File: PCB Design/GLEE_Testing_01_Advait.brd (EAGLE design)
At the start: 41.8 x 42.9 mm, 53 parts, among them IC1 SI7021, IC2 ATMEGA328-PB, IC3 PE4259, U1 V_REG_317SMD, U2 LSM9DS1, X1 LTI-SASF54GT, Y1 16MHz, Y2 32Mhz

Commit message: Final QA
Added a few changes, updated filenames, added library and BOM
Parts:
- removed C31: nc, SparkFun:0402-CAP
- added C26: 100nF, SparkFun:0402-CAP
- added R6: 220, SparkFun:0402-RES
- added R7: 360, SparkFun:0402-RES
- C1: value 26pF -> 10nF
- C10: value 10uF -> 1uF
- C11: value 10pF -> 47pF
- C12: value 0.1uF -> 1.2pF
- C13: value 10nF -> 33pF
- C14: value 0.1uF -> nc
- C15: value 100nF -> 4.7pF
- C16: value 47pF -> 1.8pF
- C18: value nc -> 1nF
- C19: value 33pF -> 47pF
- C2: value 26pF -> 0.1uF
- C20, L2: value 10nF -> nc
- C22: value 4.7pF -> 10nF
- C23: value 1.2pF -> nc
- C25: value 1.8pF -> 100nF
- C27: value 47pF -> 100nF
- C28: value 1nF -> 10pF
- C29: value nc -> 10pF
- C3: value 0.1 uF -> 0.1uF
- C4: value 1uF -> 10uF
- C6: value 10pF -> 0.1 uF
- C7, C9: value 100nF -> 26pF
- L1: value nc -> 10nH
- L3: value 10nH -> 6.2nH
- L4: value 6.2nH -> 0R
- L5: value 0R -> 10nF
- LED1: device adafruit:LED3MM -> adafruit:CHIPLED_0805
- R1: value 10K -> 1K
- R3: value 220 -> 10K
- R4: value 360 -> 10K
- U1: value V_REG_317SMD -> LSM9DS1; device SparkFun:SOT223 -> LSM9DS1:LGA24-8X4
- U2: value LSM9DS1 -> V_REG_317SMD; device LSM9DS1:LGA24-8X4 -> SparkFun:SOT223
- moved R4 33.2 mm to (34.1, 25.7)
- moved C10 29.2 mm to (5.45, 16.8), turned to 0 degrees
- moved C4 29.2 mm to (30.5, 31.9), turned to 180 degrees
- moved C6 25.9 mm to (17.3, 28.6)
- moved C14 24.5 mm to (14.3, 15.3)
- moved C29 24.0 mm to (36.6, 6.45), turned to 0 degrees
- moved U1 23.6 mm to (26.6, 31.2)
- moved U2 23.6 mm to (4.80, 22.1)
- moved C11 23.3 mm to (15.7, 16.6), turned to 180 degrees
- moved C13 18.4 mm to (28.2, 16.6)
- moved C12 18.3 mm to (21.4, 16.6), turned to 180 degrees
- moved R3 18.2 mm to (17.3, 26.7)
- moved C15 17.9 mm to (21.4, 15.2), turned to 180 degrees
- moved C7 17.7 mm to (20.1, 22.9)
- moved C9 16.8 mm to (20.1, 20.6)
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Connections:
- new net N$56: R1.2, SW1.P$2
- net +3.3V: now also C18.1, C26.1, C6.1, R2.2, R3.1, R4.2, R5.1, R6.2, U1.22, U1.23, U1.5, U1.6, U2.2; no longer C15.1, C28.1, C3.1, R1.1, R2.1, R3.2, R5.2, U1.2, U2.22, U2.23, U2.5, U2.6
- net GND: now also C23.2, C24.2, C26.2, C27.2, LED1.C, R1.1, R7.1, U1.14, U1.15, U1.16, U1.17, U1.18, U1.19, U1.20; no longer C11.2, C12.2, C13.2, C31.2, LED1.K, R4.1, SW1.P$2, U2.14, U2.15, U2.16, U2.17, U2.18, U2.19, U2.20
- net I1: now also U1.9; no longer U2.9
- net I2: now also U1.12; no longer U2.12
- net I3: now also U1.10; no longer U2.10
- net I4: now also U1.11; no longer U2.11
- net N$1: now also C19.1; no longer C24.1
- net N$10: now also L5.2; no longer L2.2
- net N$11: now also C13.1, L2.1; no longer C19.1, L1.1
- net N$12: now also C12.1, C15.1, L1.2, L3.1; no longer C22.1, C23.1, L3.2, L4.1
- net N$13: now also C13.2, L1.1; no longer C19.2, L3.1
- net N$14: now also C12.2, C16.1, L3.2; no longer C23.2, C25.1, L4.2
- net N$15: now also C23.1, L4.2; no longer C31.1, L5.2
- net N$16: now also C11.1; no longer C27.1
- net N$17: now also C3.1, U1.24; no longer C14.1, U2.24
- net N$18: now also C11.2, C14.1, L4.1; no longer C27.2, C29.1, L5.1
- net N$2: now also C22.1, C24.1, L2.2; no longer C16.1, C20.1, L1.2
- net N$22: now also R4.1
- net N$24: now also C27.1; no longer C7.1
- net N$25: now also C25.1; no longer C9.1
- net N$3: now also U2.3; no longer U1.3
- net N$4: now also C19.2; no longer C24.2
- net N$5: now also R2.1, U1.7, U1.8; no longer R5.1, U2.7, U2.8
- net N$6: now also R6.1, R7.2, U2.1; no longer R3.1, R4.2, U1.1
- net N$7: now also C20.1, L5.1; no longer C18.1, L2.1
- net N$8: now also C1.1, U1.21; no longer C13.1, U2.21
- net N$9: now also C2.1, U1.1, U1.3; no longer C12.1, U2.1, U2.3
- net SCL: now also R3.2; no longer R1.2
- net SCL1: now also U1.2; no longer U2.2
- net SDA: now also R5.2; no longer R2.2
- net SDA1: now also U1.4; no longer U2.4
- net XTA: now also C28.1; no longer C6.1
- net XTAL1: now also C7.1; no longer C1.1
- net XTAL2: now also C9.1; no longer C2.1
- net XTB: now also C29.1; no longer C11.1
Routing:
- net N$56: track 0.00 -> 2.73 mm
- net N$22: track 26.6 -> 28.8 mm
- net GND: track 66.2 -> 68.1 mm, vias 24 -> 53
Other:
- board text added: "GLEE_Testing_01"
- board text removed: "GLEE Prototype Rev A"

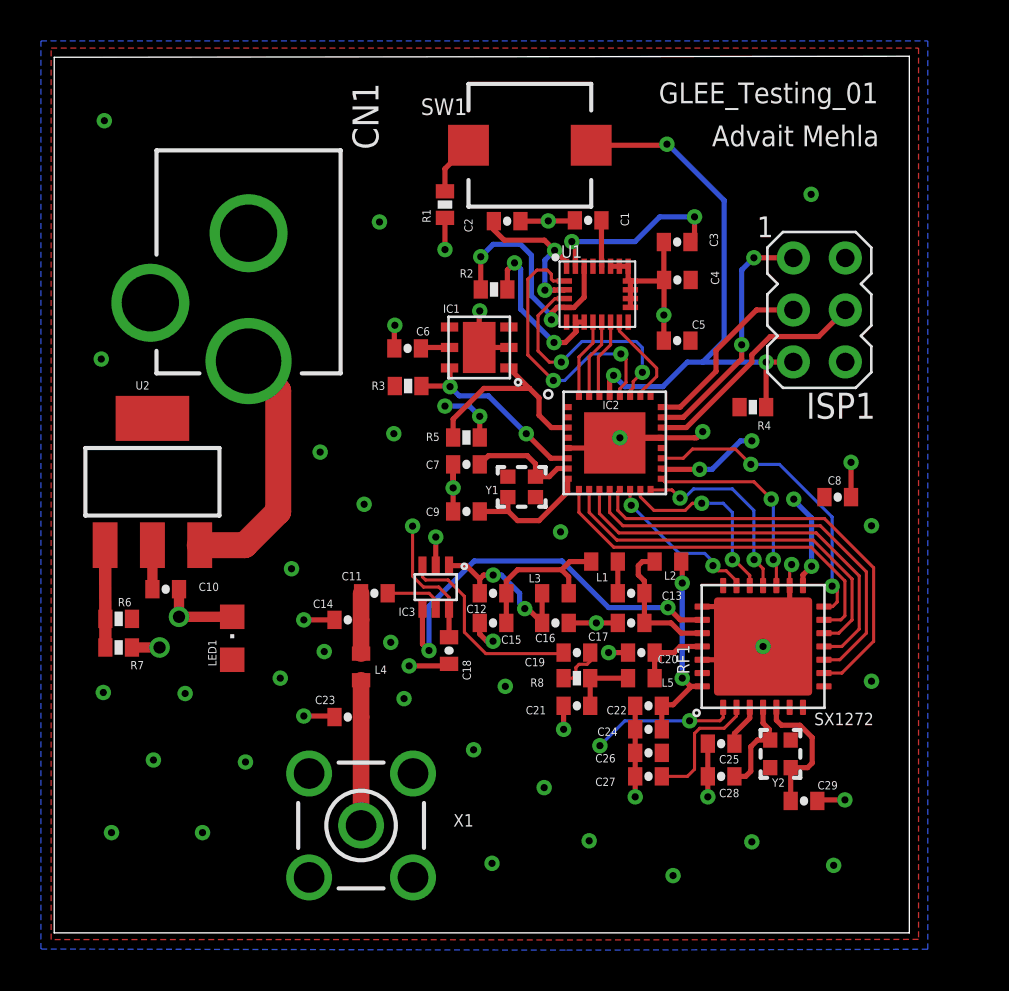
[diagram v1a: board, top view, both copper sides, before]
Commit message: Added pins for voltage testing
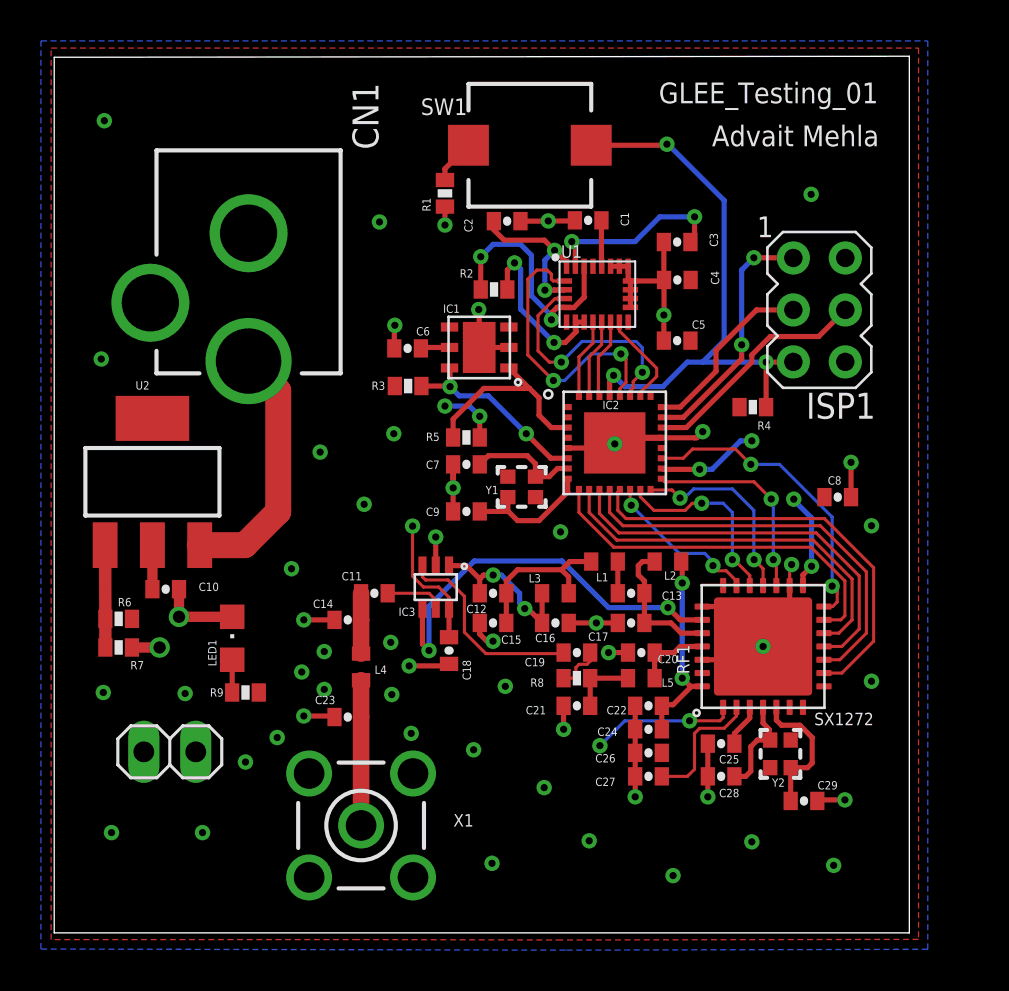
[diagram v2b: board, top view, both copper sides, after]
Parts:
- added JP6: (no value), pinhead:1X02
- added R9: 100, SparkFun:0402-RES
- moved R1 0.55 mm to (19.1, 36.1)
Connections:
- new net N$19: LED1.A, R9.1
- net +3.3V: now also JP6.2, R9.2; no longer LED1.A
- net GND: now also JP6.1
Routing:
- net N$19: track 0.00 -> 1.60 mm
- net GND: track 68.1 -> 67.2 mm, vias 53 -> 55
- net N$56: track 2.73 -> 2.18 mm
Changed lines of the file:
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@@
 <layer number="21" name="tPlace" color="7" fill="1" visible="yes" active="yes"/>
 <layer number="22" name="bPlace" color="7" fill="1" visible="yes" active="yes"/>
-<layer number="23" name="tOrigins" color="15" fill="1" visible="no" active="yes"/>
+<layer number="23" name="tOrigins" color="15" fill="1" visible="yes" active="yes"/>
 <layer number="24" name="bOrigins" color="15" fill="1" visible="no" active="yes"/>
 <layer number="25" name="tNames" color="7" fill="1" visible="yes" active="yes"/>
@@
 <attribute name="VALUE" x="35.2295" y="26.843" size="0.4064" layer="27" rot="R180"/>
 </element>
-<element name="R1" library="SparkFun" package="0402-RES" value="1K" x="19.1" y="35.6" smashed="yes" rot="R90">
-<attribute name="NAME" x="18.4015" y="34.711" size="0.4064" layer="25" rot="R90"/>
-<attribute name="VALUE" x="18.443" y="36.3705" size="0.4064" layer="27" rot="R90"/>
+<element name="R1" library="SparkFun" package="0402-RES" value="1K" x="19.1" y="36.15" smashed="yes" rot="R90">
+<attribute name="NAME" x="18.4015" y="35.261" size="0.4064" layer="25" rot="R90"/>
+<attribute name="VALUE" x="18.443" y="36.9205" size="0.4064" layer="27" rot="R90"/>
+</element>
+<element name="JP6" library="pinhead" library_urn="urn:adsk.eagle:library:325" package="1X02" package3d_urn="urn:adsk.eagle:package:22435/2" value="" x="5.65" y="8.85" smashed="yes">
+<attribute name="POPULARITY" value="98" x="5.65" y="8.85" size="1.778" layer="27" display="off"/>
+<attribute name="VALUE" x="3.11" y="5.675" size="1.27" layer="27"/>
+</element>
+<element name="R9" library="SparkFun" package="0402-RES" value="100" x="9.35" y="11.75" smashed="yes">
+<attribute name="NAME" x="7.611" y="11.5485" size="0.4064" layer="25"/>
 </element>
 </elements>
@@
 <wire x1="16.625" y1="29.675" x2="16.65" y2="29.7" width="0.254" layer="1"/>
 <via x="16.65" y="29.7" extent="1-16" drill="0.35"/>
-<wire x1="29.7" y1="24.2" x2="27.65" y2="24.2" width="0.3048" layer="1"/>
-<wire x1="27.65" y1="24.2" x2="27.4" y2="23.95" width="0.3048" layer="1"/>
+<wire x1="29.7" y1="24.2" x2="27.7" y2="24.2" width="0.3048" layer="1"/>
+<wire x1="27.7" y1="24.2" x2="27.4" y2="23.9" width="0.3048" layer="1"/>
+<wire x1="27.4" y1="23.9" x2="27.4" y2="23.95" width="0.3048" layer="1"/>
 <wire x1="27.195" y1="32.585" x2="27.625" y2="32.585" width="0.254" layer="1"/>
 <wire x1="28.055" y1="32.585" x2="27.625" y2="32.585" width="0.254" layer="1"/>
@@
 <wire x1="19.5" y1="22.9" x2="19.5" y2="20.6" width="0.254" layer="1"/>
 <via x="19.5" y="21.75" extent="1-16" drill="0.35"/>
-<wire x1="20.775" y1="28.615" x2="20.775" y2="30.375" width="0.254" layer="1"/>
-<wire x1="20.775" y1="30.375" x2="20.8" y2="30.4" width="0.254" layer="1"/>
-<via x="20.8" y="30.4" extent="1-16" drill="0.35"/>
+<wire x1="20.775" y1="28.615" x2="20.775" y2="30.4444" width="0.254" layer="1"/>
 <wire x1="35.95" y1="16.975" x2="35.95" y2="17.9079625" width="0.1524" layer="1"/>
 <wire x1="35.95" y1="17.9079625" x2="36.04601875" y2="18.00398125" width="0.1524" layer="1"/>
@@
 <wire x1="38.95" y1="23" x2="38.95" y2="21.3" width="0.254" layer="1"/>
 <via x="38.95" y="23" extent="1-16" drill="0.35"/>
-<wire x1="25.1" y1="23.7" x2="27.15" y2="23.7" width="0.254" layer="1"/>
-<wire x1="27.15" y1="23.7" x2="27.65" y2="24.2" width="0.254" layer="1"/>
-<via x="27.65" y="24.2" extent="1-16" drill="0.35"/>
+<wire x1="25.1" y1="23.7" x2="27.2" y2="23.7" width="0.254" layer="1"/>
+<wire x1="27.2" y1="23.7" x2="27.4" y2="23.9" width="0.254" layer="1"/>
+<via x="27.4" y="23.9" extent="1-16" drill="0.35"/>
 <wire x1="29.8" y1="28.95" x2="29.8" y2="30.2" width="0.254" layer="1"/>
 <via x="29.8" y="30.2" extent="1-16" drill="0.35"/>
@@
 <wire x1="8.7" y1="15.45" x2="6.1" y2="15.45" width="0.508" layer="1"/>
 <contactref element="R1" pad="1"/>
-<via x="19.1" y="33.4" extent="1-16" drill="0.35"/>
-<wire x1="19.1" y1="34.95" x2="19.1" y2="33.4" width="0.254" layer="1"/>
+<via x="19.1" y="34.6" extent="1-16" drill="0.35"/>
+<wire x1="19.1" y1="35.5" x2="19.1" y2="34.6" width="0.254" layer="1"/>
 <via x="2.45" y="39.7" extent="1-16" drill="0.35"/>
 <via x="15.9" y="34.75" extent="1-16" drill="0.35"/>
@@
 <via x="20.5" y="8.95" extent="1-16" drill="0.35"/>
 <via x="22.05" y="12.05" extent="1-16" drill="0.35"/>
-<via x="17.1" y="11.45" extent="1-16" drill="0.35"/>
+<via x="16.5" y="11.65" extent="1-16" drill="0.35"/>
 <via x="16.45" y="14.2" extent="1-16" drill="0.35"/>
 <via x="13.2" y="13.75" extent="1-16" drill="0.35"/>
-<via x="11.05" y="12.45" extent="1-16" drill="0.35"/>
+<via x="12.1" y="12.75" extent="1-16" drill="0.35"/>
 <via x="6.4" y="11.7" extent="1-16" drill="0.35"/>
 <via x="2.4" y="11.75" extent="1-16" drill="0.35"/>
-<via x="4.85" y="8.45" extent="1-16" drill="0.35"/>
+<via x="10.9" y="9.55" extent="1-16" drill="0.35"/>
 <via x="9.35" y="8.35" extent="1-16" drill="0.35"/>
 <via x="2.8" y="4.9" extent="1-16" drill="0.35"/>
 <via x="7.25" y="4.9" extent="1-16" drill="0.35"/>
+<contactref element="JP6" pad="1"/>
+<via x="17.45" y="9.75" extent="1-16" drill="0.35"/>
+<via x="13.2" y="11.9" extent="1-16" drill="0.35"/>
+<wire x1="20.775" y1="30.4444" x2="20.75" y2="30.4694" width="0.254" layer="1"/>
+<via x="20.75" y="30.4694" extent="1-16" drill="0.35"/>
 </signal>
 <signal name="SDA">
@@
 <via x="26.675" y="9.15" extent="1-16" drill="0.35"/>
 <wire x1="32.7" y1="10.525" x2="32.541575" y2="10.366575" width="0.1524" layer="1"/>
-<contactref element="LED1" pad="A"/>
 <contactref element="R4" pad="2"/>
+<contactref element="JP6" pad="2"/>
+<contactref element="R9" pad="2"/>
 </signal>
 <signal name="N$17">
@@
 <contactref element="SW1" pad="P$2"/>
 <contactref element="R1" pad="2"/>
-<wire x1="19.1" y1="36.25" x2="19.1" y2="37.35" width="0.254" layer="1"/>
+<wire x1="19.1" y1="36.8" x2="19.1" y2="37.35" width="0.254" layer="1"/>
 <wire x1="19.1" y1="37.35" x2="20.25" y2="38.5" width="0.254" layer="1"/>
 </signal>
+<signal name="N$19">
+<contactref element="LED1" pad="A"/>
+<contactref element="R9" pad="1"/>
+<wire x1="8.7" y1="11.75" x2="8.7" y2="13.35" width="0.254" layer="1"/>
+</signal>
 </signals>
